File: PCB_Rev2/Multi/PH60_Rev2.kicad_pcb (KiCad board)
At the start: 2 copper layers, 285 x 94.6 mm, 176 parts, among them J1 USB_C_Receptacle_USB2.0_16P, J2 Conn_01x02, U2 W25Q128JVS, U3 RP2040, U4 XC6206PxxxMR, Y1 Crystal_GND24

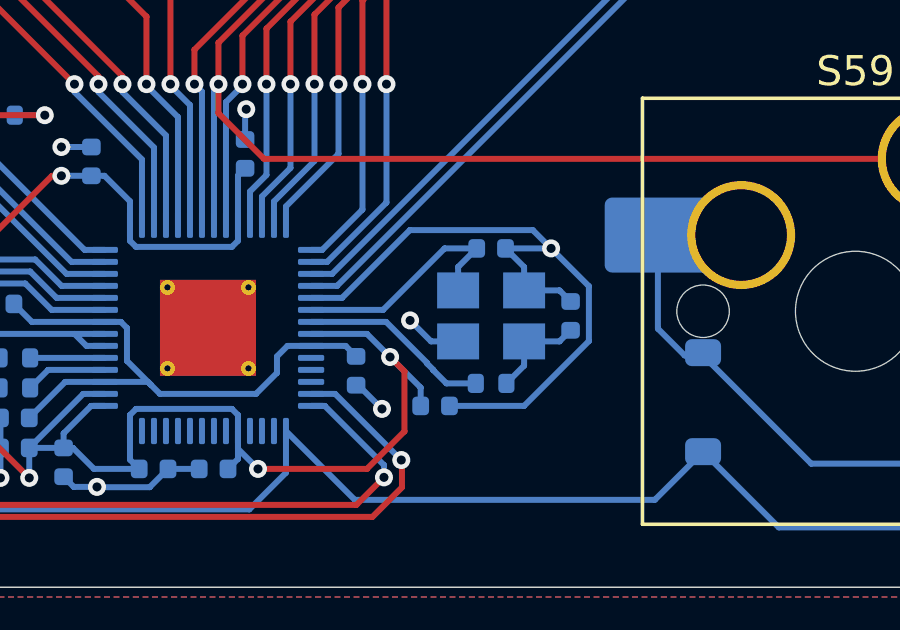
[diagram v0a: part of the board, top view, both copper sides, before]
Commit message: Add GND Through Hole for Crystal
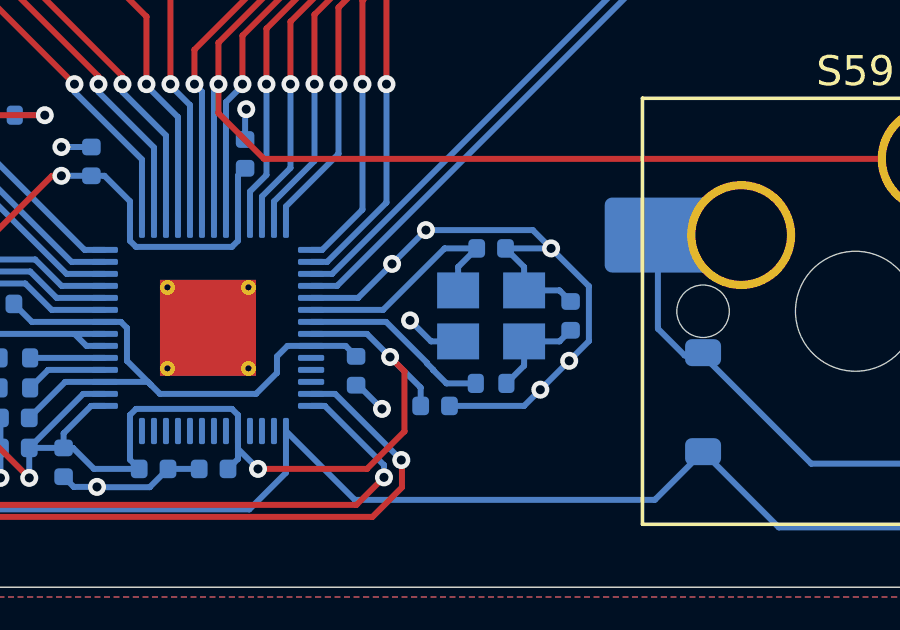
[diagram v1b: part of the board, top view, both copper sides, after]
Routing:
- net GND: vias 12 -> 16
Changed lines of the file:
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@@
+	)
+	(via
+		(at 149.039264 116.914264)
+		(size 0.6)
+		(drill 0.3)
+		(layers "F.Cu" "B.Cu")
+		(net 1)
 	)
 	(via
@@
 	)
 	(via
+		(at 150.001764 115.951764)
+		(size 0.6)
+		(drill 0.3)
+		(layers "F.Cu" "B.Cu")
+		(net 1)
+	)
+	(via
 		(at 134.261029 120.155)
 		(size 0.6)
@@
 	)
 	(via
+		(at 145.225 111.595)
+		(size 0.6)
+		(drill 0.3)
+		(layers "F.Cu" "B.Cu")
+		(net 1)
+	)
+	(via
 		(at 143.761029 117.555)
+		(size 0.6)
+		(drill 0.3)
+		(layers "F.Cu" "B.Cu")
+		(net 1)
+	)
+	(via
+		(at 144.0975 112.7225)
 		(size 0.6)
 		(drill 0.3)
@@
 	)
 	(segment
+		(start 148.498529 117.455)
+		(end 149.039264 116.914264)
+		(width 0.2)
+		(layer "B.Cu")
+		(net 1)
+	)
+	(segment
 		(start 131.043529 118.855)
 		(end 131.043529 117.855)
@@
 	)
 	(segment
-		(start 142.429447 113.855)
-		(end 141.398529 113.855)
-		(width 0.2)
-		(layer "B.Cu")
-		(net 1)
-	)
-	(segment
-		(start 144.689447 111.595)
-		(end 142.429447 113.855)
-		(width 0.2)
-		(layer "B.Cu")
-		(net 1)
-	)
-	(segment
 		(start 144.697794 114.605735)
 		(end 145.397059 115.305)
@@
 	)
 	(segment
+		(start 145.225 111.595)
+		(end 142.965 113.855)
+		(width 0.2)
+		(layer "B.Cu")
+		(net 1)
+	)
+	(segment
 		(start 134.271029 120.165)
 		(end 136.018529 120.165)
@@
 	)
 	(segment
-		(start 148.498529 117.455)
-		(end 150.658529 115.295)
-		(width 0.2)
-		(layer "B.Cu")
-		(net 1)
-	)
-	(segment
 		(start 50.35 36.255)
 		(end 50.35 37.415)
@@
 	)
 	(segment
+		(start 148.788529 111.595)
+		(end 145.225 111.595)
+		(width 0.2)
+		(layer "B.Cu")
+		(net 1)
+	)
+	(segment
 		(start 149.678529 113.605)
 		(end 150.048529 113.975)
@@
 	)
 	(segment
+		(start 149.039264 116.914264)
+		(end 150.001764 115.951764)
+		(width 0.2)
+		(layer "B.Cu")
+		(net 1)
+	)
+	(segment
+		(start 142.965 113.855)
+		(end 141.398529 113.855)
+		(width 0.2)
+		(layer "B.Cu")
+		(net 1)
+	)
+	(segment
 		(start 148.498529 113.605)
 		(end 149.678529 113.605)
@@
 	)
 	(segment
-		(start 148.788529 111.595)
-		(end 144.689447 111.595)
-		(width 0.2)
-		(layer "B.Cu")
-		(net 1)
-	)
-	(segment
 		(start 43.95 36.915)
 		(end 45.9 38.865)
@@
 	)
 	(segment
+		(start 43.95 36.255)
+		(end 43.95 36.915)
+		(width 0.2)
+		(layer "B.Cu")
+		(net 1)
+	)
+	(segment
+		(start 150.001764 115.951764)
+		(end 150.658529 115.295)
+		(width 0.2)
+		(layer "B.Cu")
+		(net 1)
+	)
+	(segment
 		(start 149.398529 112.205)
 		(end 148.788529 111.595)
 		(width 0.2)
 		(layer "B.Cu")
-		(net 1)
-	)
-	(segment
-		(start 43.95 36.255)
-		(end 43.95 36.915)
-		(width 0.2)
-		(layer "B.Cu")

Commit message: Wiring Improvement
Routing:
- net +3V3: track 91.3 -> 93.8 mm, vias 6 -> 5
- net /USB_D-: track 144.3 -> 143.2 mm
- net /USB_D+: track 144.5 -> 143.4 mm
- net row_3: track 306.0 -> 305.1 mm
- net row_2: track 346.9 -> 346.0 mm
- added copper zone on B.Cu, net GND
- removed copper zone on B.Cu, net (none)

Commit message: Tinkering
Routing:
- net col_13: track 325.8 -> 318.4 mm
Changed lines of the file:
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@@
 	)
 	(segment
-		(start 283.21 43.18)
-		(end 283.15 43.12)
+		(start 283.21 37.316598)
+		(end 284.966598 35.56)
 		(width 0.2)
 		(layer "B.Cu")
@@
 	)
 	(segment
-		(start 283.15 43.12)
-		(end 283.15 37.376598)
+		(start 283.21 43.18)
+		(end 283.15 43.12)
 		(width 0.2)
 		(layer "B.Cu")
@@
 	)
 	(segment
-		(start 283.15 37.376598)
-		(end 284.966598 35.56)
+		(start 283.21 43.18)
+		(end 283.21 37.316598)
 		(width 0.2)
 		(layer "B.Cu")
@@
 	)
 	(segment
-		(start 297.875 33.08)
-		(end 297.875 38.795)
-		(width 0.2)
-		(layer "F.Cu")
-		(net 97)
-	)
-	(segment
 		(start 146.818139 100.8)
 		(end 199.256917 100.8)
@@
 	)
 	(segment
-		(start 297.875 38.795)
-		(end 302.26 43.18)
-		(width 0.2)
-		(layer "F.Cu")
-		(net 97)
-	)
-	(segment
 		(start 257.258035 119.34)
 		(end 259.548035 117.05)
@@
 	)
 	(segment
-		(start 296.058402 40.64)
-		(end 292.335 40.64)
-		(width 0.2)
-		(layer "B.Cu")
-		(net 97)
-	)
-	(segment
 		(start 308.98875 110.47)
 		(end 308.98875 116.24875)
@@
 	)
 	(segment
-		(start 297.875 33.08)
-		(end 297.875 38.823402)
+		(start 297.815 38.883402)
+		(end 296.058402 40.64)
 		(width 0.2)
 		(layer "B.Cu")
@@
 	(segment
 		(start 297.815 33.02)
+		(end 297.815 38.883402)
+		(width 0.2)
+		(layer "B.Cu")
+		(net 97)
+	)
+	(segment
+		(start 297.815 33.02)
 		(end 297.875 33.08)
 		(width 0.2)
@@
 	)
 	(segment
-		(start 297.875 38.823402)
+		(start 296.94 40.64)
 		(end 296.058402 40.64)
 		(width 0.2)
 		(layer "B.Cu")
+		(net 97)
+	)
+	(segment
+		(start 299.48 43.18)
+		(end 296.94 40.64)
+		(width 0.2)
+		(layer "B.Cu")
+		(net 97)
+	)
+	(segment
+		(start 296.058402 40.64)
+		(end 292.335 40.64)
+		(width 0.2)
+		(layer "B.Cu")

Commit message: Wiring Improvement
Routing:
- net col_13: track 318.4 -> 304.6 mm
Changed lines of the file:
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@@
 	)
 	(segment
-		(start 160.1025 73.66)
-		(end 160.3825 73.94)
+		(start 162.2075 77.58)
+		(end 161.6075 77.58)
 		(width 0.2)
 		(layer "B.Cu")
@@
 	)
 	(segment
-		(start 160.3825 77.060965)
-		(end 160.996535 77.675)
+		(start 162.8775 73.66)
+		(end 162.8775 76.91)
 		(width 0.2)
 		(layer "B.Cu")
@@
 	)
 	(segment
-		(start 160.3825 73.94)
-		(end 160.3825 77.060965)
+		(start 160.1025 73.66)
+		(end 160.25 73.8075)
 		(width 0.2)
 		(layer "B.Cu")
@@
 	)
 	(segment
-		(start 160.996535 77.675)
-		(end 161.6075 77.675)
+		(start 162.8775 76.91)
+		(end 162.2075 77.58)
 		(width 0.2)
 		(layer "B.Cu")
@@
 	)
 	(segment
-		(start 70.425 100.146801)
-		(end 74.217621 103.939422)
+		(start 61.65 68.4318)
+		(end 61.65 81.9568)
 		(width 0.2)
 		(layer "F.Cu")
@@
 	)
 	(segment
-		(start 61.65 81.9568)
-		(end 70.425 90.7318)
+		(start 56.7 63.4818)
+		(end 61.65 68.4318)
 		(width 0.2)
 		(layer "F.Cu")
@@
 	)
 	(segment
-		(start 61.65 68.4318)
-		(end 61.65 81.9568)
+		(start 71.025 100.746801)
+		(end 74.217621 103.939422)
 		(width 0.2)
 		(layer "F.Cu")
@@
 	)
 	(segment
-		(start 47.9 38.255)
-		(end 47.625001 38.529999)
+		(start 71.025 91.3318)
+		(end 71.025 100.746801)
 		(width 0.2)
 		(layer "F.Cu")
@@
 	)
 	(segment
-		(start 70.425 90.7318)
-		(end 70.425 100.146801)
+		(start 74.217621 103.939422)
+		(end 74.500464 103.939422)
 		(width 0.2)
 		(layer "F.Cu")
@@
 	)
 	(segment
-		(start 74.217621 103.939422)
-		(end 74.500464 103.939422)
+		(start 47.625001 38.529999)
+		(end 47.625001 42.731801)
 		(width 0.2)
 		(layer "F.Cu")
@@
 	)
 	(segment
-		(start 47.625001 38.529999)
-		(end 47.625001 42.731801)
+		(start 47.9 38.255)
+		(end 47.625001 38.529999)
 		(width 0.2)
 		(layer "F.Cu")
@@
 	)
 	(segment
-		(start 56.7 63.4818)
-		(end 61.65 68.4318)
+		(start 56.7 51.8068)
+		(end 56.7 63.4818)
 		(width 0.2)
 		(layer "F.Cu")
@@
 	)
 	(segment
-		(start 56.7 51.8068)
-		(end 56.7 63.4818)
+		(start 61.65 81.9568)
+		(end 71.025 91.3318)
 		(width 0.2)
 		(layer "F.Cu")
@@
 	)
 	(segment
-		(start 61.2 68.6182)
-		(end 61.2 82.1432)
+		(start 56.25 51.9932)
+		(end 56.25 63.6682)
 		(width 0.2)
 		(layer "F.Cu")
@@
 	)
 	(segment
-		(start 61.2 82.1432)
-		(end 69.975 90.9182)
+		(start 61.2 68.6182)
+		(end 61.2 82.1432)
 		(width 0.2)
 		(layer "F.Cu")
@@
 	)
 	(segment
-		(start 56.25 51.9932)
-		(end 56.25 63.6682)
+		(start 73.899422 104.257621)
+		(end 73.899422 104.540464)
 		(width 0.2)
 		(layer "F.Cu")
@@
 	)
 	(segment
-		(start 47.174999 38.529999)
-		(end 47.174999 42.918199)
+		(start 46.9 38.255)
+		(end 47.174999 38.529999)
 		(width 0.2)
 		(layer "F.Cu")
@@
 	)
 	(segment
-		(start 47.174999 42.918199)
-		(end 56.25 51.9932)
+		(start 61.2 82.1432)
+		(end 70.575 91.5182)
 		(width 0.2)
 		(layer "F.Cu")
@@
 	)
 	(segment
-		(start 73.899422 104.257621)
-		(end 73.899422 104.540464)
+		(start 70.575 91.5182)
+		(end 70.575 100.933199)
 		(width 0.2)
 		(layer "F.Cu")
@@
 	)
 	(segment
-		(start 56.25 63.6682)
-		(end 61.2 68.6182)
+		(start 47.174999 42.918199)
+		(end 56.25 51.9932)
 		(width 0.2)
 		(layer "F.Cu")
@@
 	)
 	(segment
-		(start 69.975 100.333199)
-		(end 73.899422 104.257621)
+		(start 47.174999 38.529999)
+		(end 47.174999 42.918199)
 		(width 0.2)
 		(layer "F.Cu")
@@
 	)
 	(segment
-		(start 69.975 90.9182)
-		(end 69.975 100.333199)
+		(start 56.25 63.6682)
+		(end 61.2 68.6182)
 		(width 0.2)
 		(layer "F.Cu")
@@
 	)
 	(segment
-		(start 46.9 38.255)
-		(end 47.174999 38.529999)
+		(start 70.575 100.933199)
+		(end 73.899422 104.257621)
 		(width 0.2)
 		(layer "F.Cu")
@@
 	)
 	(segment
-		(start 289.56 40.64)
-		(end 292.1 43.18)
-		(width 0.2)
-		(layer "F.Cu")
-		(net 97)
-	)
-	(segment
 		(start 199.256917 100.8)
 		(end 217.867917 119.411)
@@
 		(width 0.2)
 		(layer "F.Cu")
-		(net 97)
-	)
-	(segment
-		(start 292.1 43.18)
-		(end 302.26 43.18)
-		(width 0.2)
-		(layer "F.Cu")
